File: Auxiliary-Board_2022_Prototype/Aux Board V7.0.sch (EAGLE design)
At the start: 56 parts, among them CON11 1X01, CON12 1X01, CON13 1X01, CON14 1X01, CON15 1X01, CON16 1X01, CON17 1X01, CON18 1X01, CON5 1X01, CON8 1X01, IC1 RS232-TTL_MAX232E

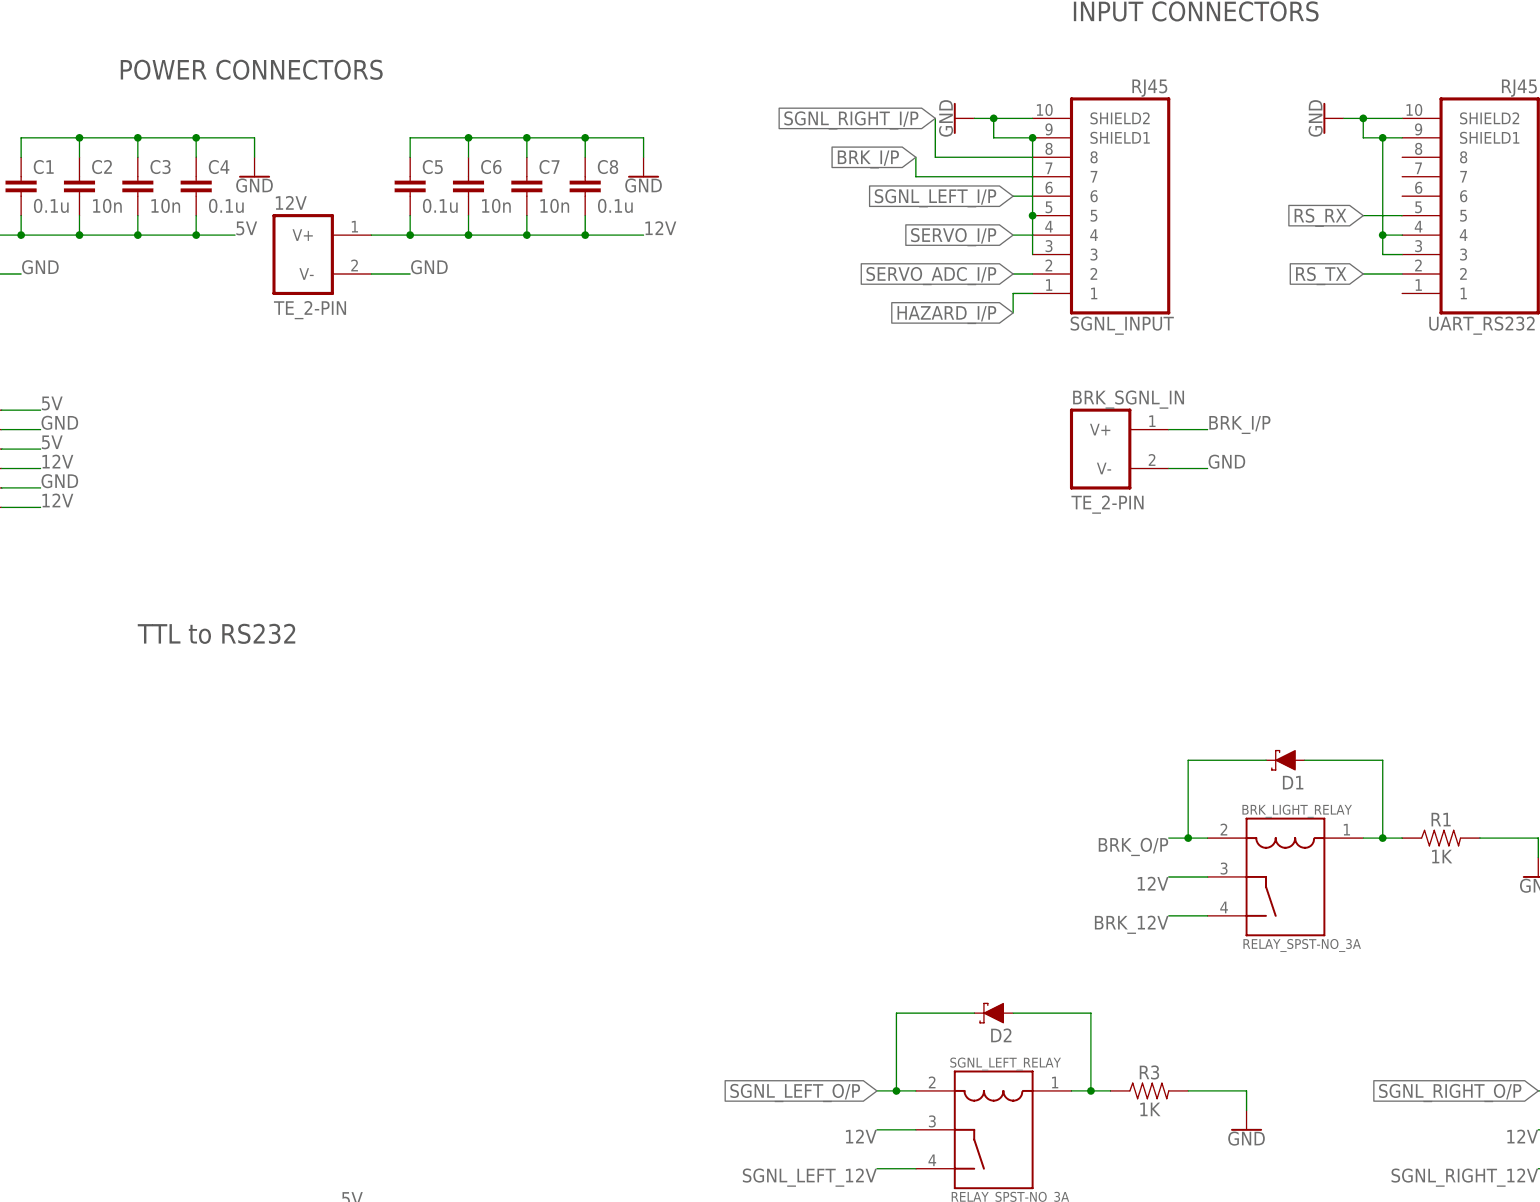
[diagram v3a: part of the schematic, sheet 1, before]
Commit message: fix: correct RS232 pins
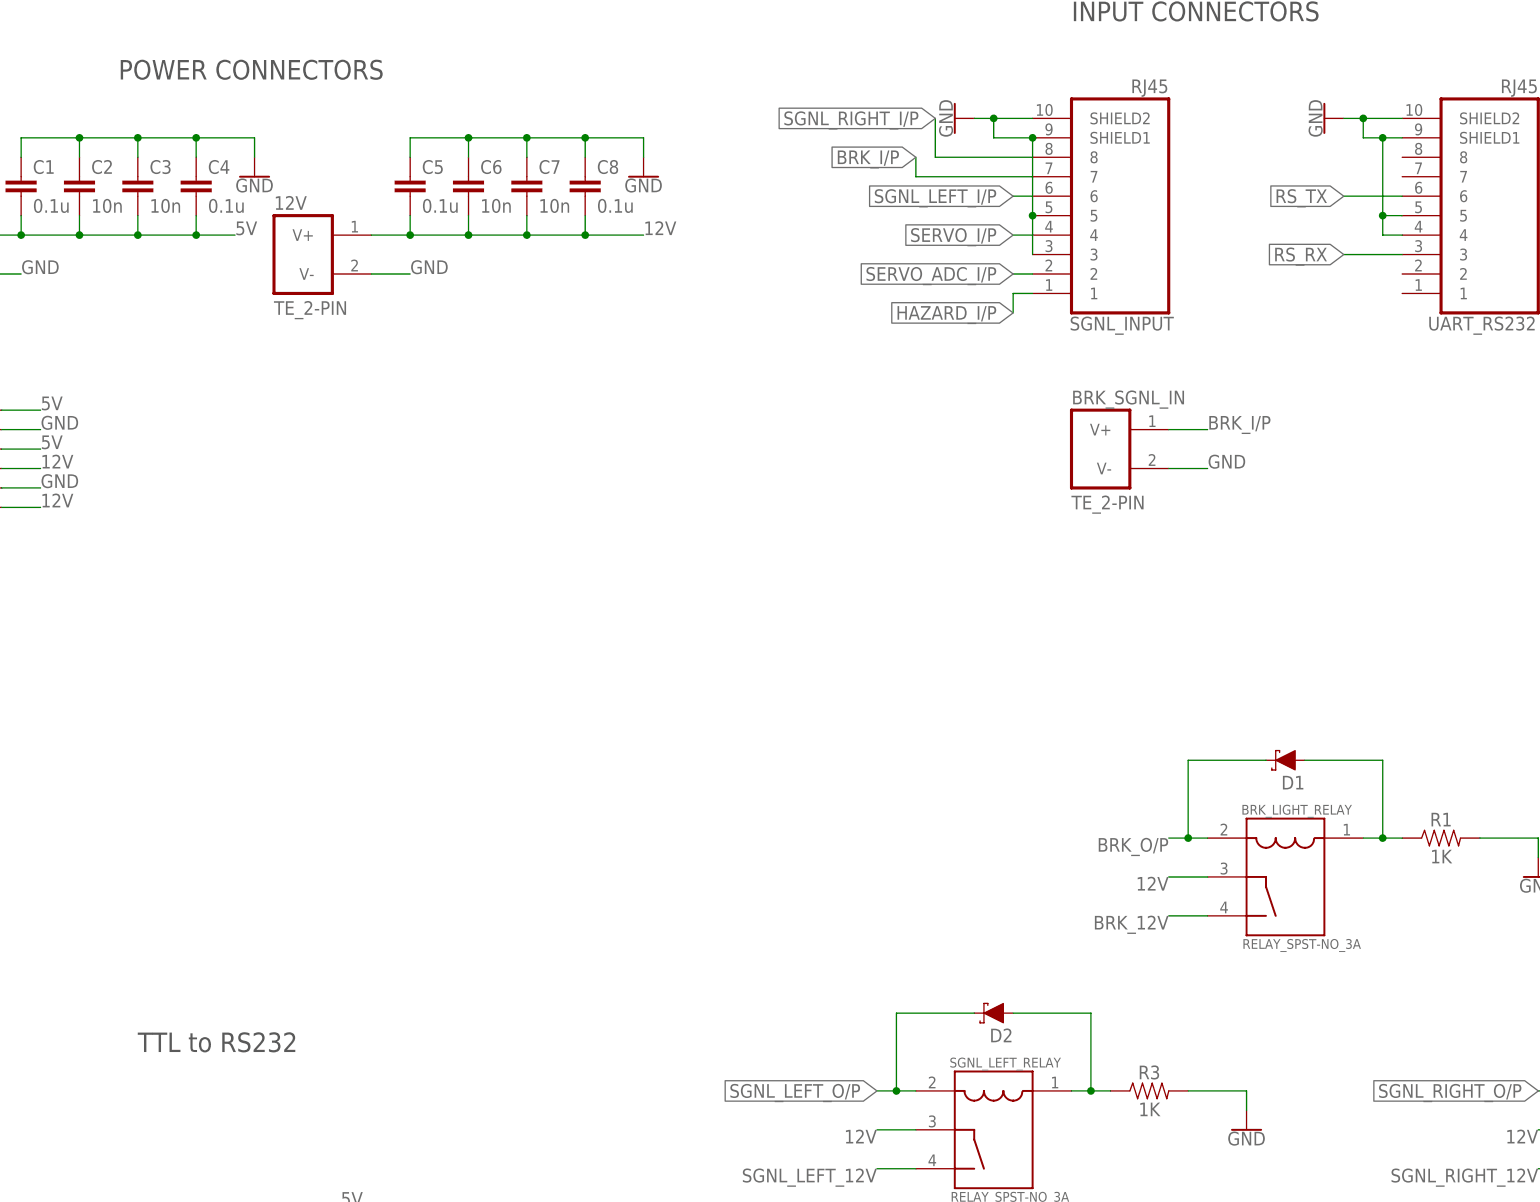
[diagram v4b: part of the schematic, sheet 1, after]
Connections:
- net GND: now also UART_RS232.5; no longer UART_RS232.3
- net RS_RX: now also UART_RS232.3; no longer UART_RS232.5
- net RS_TX: now also UART_RS232.6; no longer UART_RS232.2
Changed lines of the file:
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@@
 <text x="-15.24" y="-50.8" size="1.778" layer="94" rot="R180" align="center-right">X</text>
 <text x="-15.24" y="-53.34" size="1.778" layer="94" rot="R180" align="center-right">X</text>
-<text x="-43.18" y="60.96" size="2.54" layer="97">TTL to RS232</text>
+<text x="-43.18" y="7.62" size="2.54" layer="97">TTL to RS232</text>
 </plain>
 <instances>
@@
 <junction x="116.84" y="129.54"/>
 <pinref part="GND16" gate="1" pin="GND"/>
-<pinref part="UART_RS232" gate="G$1" pin="3"/>
-<wire x1="121.92" y1="111.76" x2="119.38" y2="111.76" width="0.1524" layer="91"/>
-<wire x1="119.38" y1="111.76" x2="119.38" y2="114.3" width="0.1524" layer="91"/>
 <pinref part="UART_RS232" gate="G$1" pin="4"/>
-<wire x1="119.38" y1="114.3" x2="121.92" y2="114.3" width="0.1524" layer="91"/>
-<wire x1="119.38" y1="114.3" x2="119.38" y2="127" width="0.1524" layer="91"/>
-<junction x="119.38" y="114.3"/>
+<wire x1="121.92" y1="114.3" x2="119.38" y2="114.3" width="0.1524" layer="91"/>
+<wire x1="119.38" y1="114.3" x2="119.38" y2="116.84" width="0.1524" layer="91"/>
+<pinref part="UART_RS232" gate="G$1" pin="5"/>
+<wire x1="119.38" y1="116.84" x2="121.92" y2="116.84" width="0.1524" layer="91"/>
+<wire x1="119.38" y1="116.84" x2="119.38" y2="127" width="0.1524" layer="91"/>
+<junction x="119.38" y="116.84"/>
 <junction x="119.38" y="127"/>
 </segment>
@@
 <net name="RS_TX" class="0">
 <segment>
-<pinref part="UART_RS232" gate="G$1" pin="2"/>
-<wire x1="121.92" y1="109.22" x2="116.84" y2="109.22" width="0.1524" layer="91"/>
-<label x="116.84" y="109.22" size="1.778" layer="95" rot="R180" xref="yes"/>
-</segment>
-<segment>
 <pinref part="IC1" gate="G$1" pin="DOUT1"/>
 <wire x1="-15.24" y1="-40.64" x2="-12.7" y2="-40.64" width="0.1524" layer="91"/>
 <label x="-12.7" y="-40.64" size="1.778" layer="95" xref="yes"/>
 </segment>
+<segment>
+<pinref part="UART_RS232" gate="G$1" pin="6"/>
+<wire x1="121.92" y1="119.38" x2="114.3" y2="119.38" width="0.1524" layer="91"/>
+<label x="114.3" y="119.38" size="1.778" layer="95" rot="R180" xref="yes"/>
+</segment>
 </net>
 <net name="RS_RX" class="0">
-<segment>
-<pinref part="UART_RS232" gate="G$1" pin="5"/>
-<wire x1="121.92" y1="116.84" x2="116.84" y2="116.84" width="0.1524" layer="91"/>
-<label x="116.84" y="116.84" size="1.778" layer="95" rot="R180" xref="yes"/>
-</segment>
 <segment>
 <pinref part="IC1" gate="G$1" pin="ROUT1"/>
@@
 <label x="-12.7" y="-45.72" size="1.778" layer="95" xref="yes"/>
 </segment>
-</net>
+<segment>
+<pinref part="UART_RS232" gate="G$1" pin="3"/>
+<wire x1="121.92" y1="111.76" x2="114.3" y2="111.76" width="0.1524" layer="91"/>
+<label x="114.3" y="111.76" size="1.778" layer="95" rot="R180" xref="yes"/>
+</segment>
+</net>
